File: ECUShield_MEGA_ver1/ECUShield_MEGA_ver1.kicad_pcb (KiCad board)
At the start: 2 copper layers, 101.6 x 53.3 mm, 53 parts, among them J1 Conn_02x03_Odd_Even, J10 PWM, J11 PWM, J12 Communication, J13 Conn_01x02_Pin, J14 Conn_01x02_Pin, J15 Conn_01x02_Pin, J16 Conn_01x02_Pin, J17 Conn_01x02_Pin, J18 Conn_01x02_Pin, J19 Conn_01x02_Pin, J2 Conn_01x02_Pin, J20 Conn_01x02_Pin, J3 Conn_01x02_Pin, J4 Conn_01x03_Pin, J5 Conn_01x03_Pin, J6 Conn_01x02_Pin, J7 Power, J8 Analog, J9 Analog, K1 G5Q-1, K2 G5Q-1, Q1 MTN2306AN3, Q2 MTN2306AN3, Q3 MTN2306AN3, Q4 MTN2306AN3, U1 MCP2515-xST, U2 MCP2551-I-SN, Y1 CSTCE16M0V53-R0

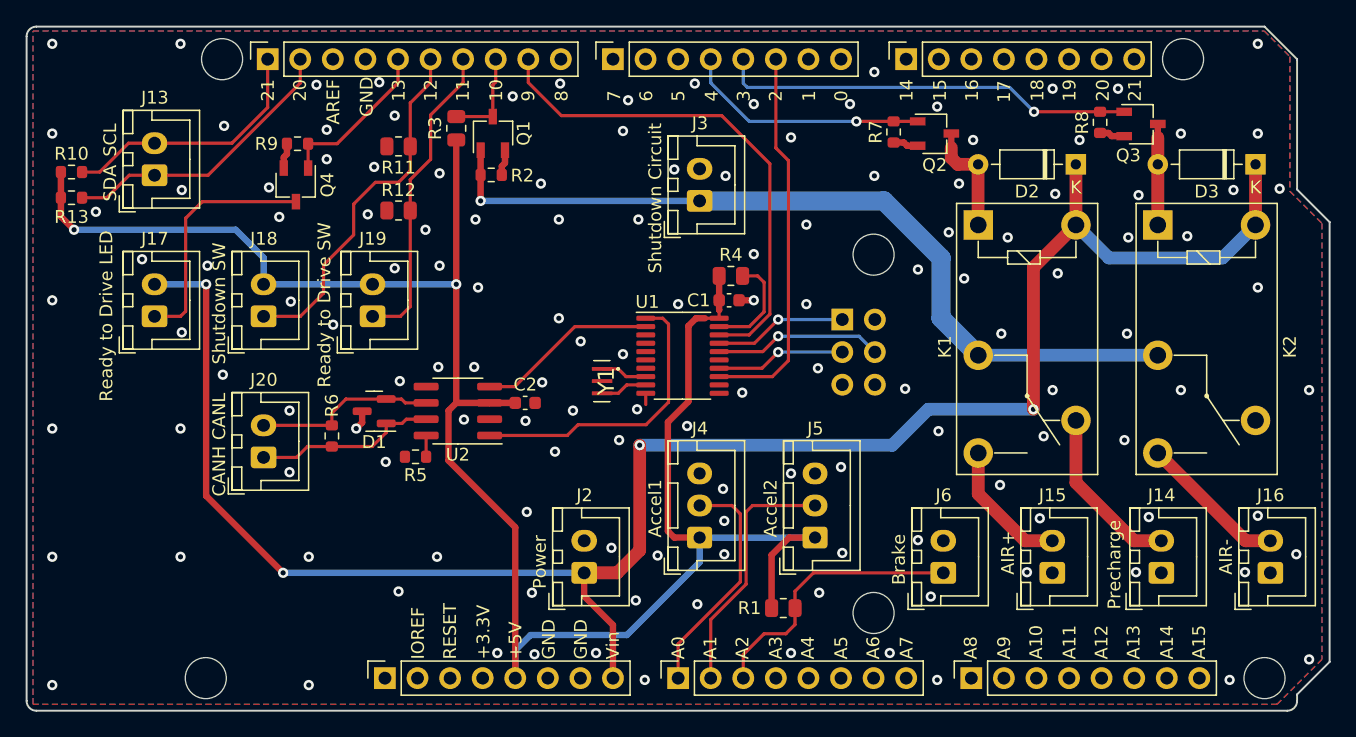
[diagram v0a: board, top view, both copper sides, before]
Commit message: 回路図修正, パターン再設計
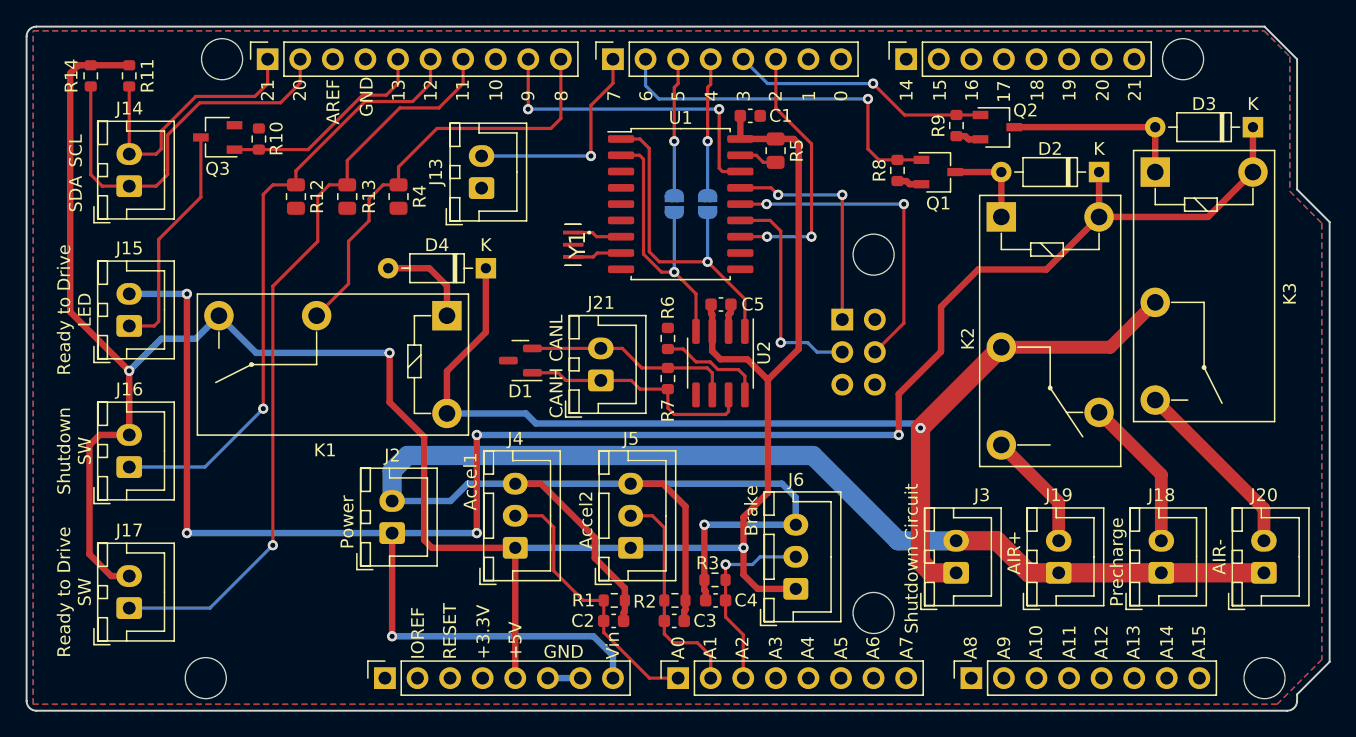
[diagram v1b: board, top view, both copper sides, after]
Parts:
- removed the K2 at (188.2, 62.1)
- removed the Q1 at (136.3, 55.0)
- added C2: 0.1u, Capacitor_SMD:C_0603_1608Metric, F.Cu at (145.8, 93.0)
- added C3: 0.1u, Capacitor_SMD:C_0603_1608Metric, F.Cu at (150.5, 93.0)
- added C4: 0.1u, Capacitor_SMD:C_0603_1608Metric, F.Cu at (153.7, 91.4)
- added D4: 1S953, Diode_THT:D_DO-35_SOD27_P7.62mm_Horizontal, F.Cu at (135.8, 65.5)
- added J13: Conn_01x02_Pin, Connector_JST:JST_XH_B2B-XH-A_1x02_P2.50mm_Vertical, F.Cu at (135.5, 59.2)
- added JP1: SolderJumper_2_Open, Jumper:SolderJumper-2_P1.3mm_Open_RoundedPad1.0x1.5mm, B.Cu at (150.5, 60.5)
- added JP2: SolderJumper_2_Open, Jumper:SolderJumper-2_P1.3mm_Open_RoundedPad1.0x1.5mm, B.Cu at (153.1, 60.5)
- added K1: G5Q-1A, Relay_THT:Relay_SPST_Omron-G5Q-1A, F.Cu at (132.8, 69.2)
- added K3: G5Q-1A, Relay_THT:Relay_SPST_Omron-G5Q-1A, F.Cu at (188.0, 58.0)
- added R4: 10k, Resistor_SMD:R_0805_2012Metric, F.Cu at (129.0, 59.9)
- J6: value Conn_01x02_Pin -> Conn_01x03_Pin; footprint Connector_JST:JST_XH_B2B-XH-A_1x02_P2.50mm_Vertical -> Connector_JST:JST_XH_B3B-XH-A_1x03_P2.50mm_Vertical
- R1, R3: value 10k -> 100k; footprint Resistor_SMD:R_0805_2012Metric -> Resistor_SMD:R_0603_1608Metric
- R2: value 1M -> 100k
- U1: value MCP2515-xST -> MCP2515-xSO; footprint Package_SO:TSSOP-20_4.4x6.5mm_P0.65mm -> Package_SO:SOIC-18W_7.5x11.6mm_P1.27mm
- moved R3 40.6 mm to (153.7, 89.8), turned to 180 degrees
- moved R2 36.1 mm to (150.6, 91.4)
- moved J3 35.2 mm to (172.5, 89.2)
- moved J17 29.6 mm to (108.0, 92.0)
- moved J21 27.0 mm to (144.8, 74.2)
- moved R7 26.6 mm to (150.0, 74.1)
- moved R6 21.7 mm to (150.0, 71.0), turned to 90 degrees
- moved U2 20.8 mm to (154.1, 72.9), turned to -90 degrees
- moved C5 17.1 mm to (154.1, 68.3)
- moved J16 15.7 mm to (108.0, 81.0)
- moved J2 15.3 mm to (128.5, 86.2)
- moved C1 14.5 mm to (156.4, 53.6)
- moved J4 14.4 mm to (138.1, 87.3)
- moved J5 14.4 mm to (147.1, 87.3)
- moved R1 13.2 mm to (145.8, 91.4)
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- renumbered C2 to C5, J13 to J14, J17 to J15, J18 to J16, J19 to J17, J14 to J18, J15 to J19, J16 to J20, J20 to J21, K1 to K2, Q2 to Q1, Q3 to Q2, Q4 to Q3, R9 to R10, R10 to R11, R11 to R12, R12 to R13, R13 to R14, R4 to R5, R5 to R6, R6 to R7, R7 to R8, R8 to R9
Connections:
- J6 pad 1: /A2 -> +5V
- J6 pad 2: GND -> /A2
- Q1 pad 1: /*4 -> /*6
- R1 pad 1: +5V -> /A0
- R1 pad 2: /A2 -> GND
- R2 pad 1: SHUTDOWN_CIRCUIT -> /A1
- R3 pad 1: +5V -> /A2
- R3 pad 2: /*10 -> GND
- R8 pad 1: /*4 -> /*6
- U1 pad 10: GND -> unconnected-(U1-~{RX1BF}-Pad10)
- U1 pad 12: unconnected-(U1-~{RX0BF}-Pad12) -> /*2/INT_A
- U1 pad 13: /*2/INT_A -> /SCK_A
- U1 pad 14: /SCK_A -> /MOSI_A
- U1 pad 15: unconnected-(U1-NC-Pad15) -> /MISO_A
- U1 pad 16: /MOSI_A -> /*9/CS_A
- U1 pad 17: /MISO_A -> Net-(U1-~{RESET})
- U1 pad 18: /*9/CS_A -> +5V
- U1 pad 7: unconnected-(U1-~{TX2RTS}-Pad7) -> /OSC2
- U1 pad 8: /OSC2 -> /OSC1
- U1 pad 9: /OSC1 -> GND
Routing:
- net GND: track 11.6 -> 167.9 mm, vias 139 -> 1
- net /*11: track 24.2 -> 59.9 mm, vias 0 -> 1
- net /*8: track 0.00 -> 33.8 mm
- net +5V: track 150.4 -> 180.4 mm, vias 2 -> 3
- net /*6: track 0.00 -> 28.3 mm, vias 0 -> 1
- net SHUTDOWN_CIRCUIT: track 64.5 -> 85.9 mm
- net /*12: track 28.2 -> 48.2 mm, vias 0 -> 1
- net /*7: track 0.00 -> 16.8 mm, vias 0 -> 1
- net /*9/CS_A: track 39.6 -> 25.2 mm, vias 0 -> 2
- net +12V: track 148.1 -> 161.0 mm, vias 4 -> 6
- net /*3: track 32.5 -> 20.3 mm
- net /MOSI_A: track 13.2 -> 25.2 mm, vias 1 -> 2
- net /*5: track 0.00 -> 10.8 mm, vias 0 -> 1
- net /*2/INT_A: track 29.8 -> 20.5 mm, vias 0 -> 2
- net /*4: track 19.2 -> 10.7 mm
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
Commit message: パターン再設計完了, 寝かせ
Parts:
- moved J2 22.7 mm to (151.0, 89.2)
- moved C2 15.5 mm to (130.9, 88.5)
- moved R1 15.5 mm to (131.0, 86.9)
- moved J4 13.0 mm to (125.5, 90.5)
- moved R3 11.5 mm to (165.1, 88.0), turned to 0 degrees
- moved C4 11.4 mm to (165.0, 89.6), turned to 0 degrees
- moved J5 8.27 mm to (139.5, 90.5)
- moved C3 6.51 mm to (144.9, 89.6)
- moved R2 6.51 mm to (145.0, 88.0)
- moved J6 0.50 mm to (159.5, 90.5)
- moved R14 0.50 mm to (105.5, 50.5)
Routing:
- net GND: track 167.9 -> 135.4 mm, vias 1 -> 116
- net +12V: track 161.0 -> 147.7 mm, vias 6 -> 5
- net /A0: track 21.4 -> 33.9 mm, vias 0 -> 2
- net +5V: track 180.4 -> 190.8 mm
- net /A1: track 17.4 -> 21.5 mm, vias 0 -> 2
- net /A2: track 15.2 -> 18.6 mm, vias 1 -> 0
- net /*11: track 59.9 -> 61.3 mm
- net /*6: track 28.3 -> 26.9 mm
- net /*3: track 20.3 -> 21.4 mm
- net /MOSI_A: track 25.2 -> 24.2 mm
- net /SDA/20: track 30.6 -> 29.7 mm
- net /SCL/21: track 21.1 -> 20.3 mm
- net /MISO_A: track 17.9 -> 17.2 mm
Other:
- board text added: "5V"
- board text removed: "+5V"

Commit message: 修正版寝かせ
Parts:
- added J22: Conn_01x02_Pin, Connector_JST:JST_XH_B2B-XH-A_1x02_P2.50mm_Vertical, F.Cu at (129.5, 59.2)
- moved R12 7.50 mm to (115.0, 64.4)
- moved R13 6.73 mm to (120.0, 64.4)
- moved R4 6.02 mm to (125.0, 64.4)
- moved J13 1.30 mm to (136.8, 59.2)
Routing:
- net /*10: track 0.00 -> 12.7 mm
- net /*12: track 48.2 -> 56.3 mm
- net /*8: track 33.6 -> 37.4 mm, vias 0 -> 2
- net /MOSI_A: track 24.2 -> 20.8 mm
- net /*11: track 61.3 -> 64.0 mm
- net GND: track 135.4 -> 133.1 mm, vias 116 -> 117
- net /*7: track 16.8 -> 15.5 mm
- net /*2/INT_A: track 20.5 -> 19.3 mm
- net /*13: track 16.8 -> 17.9 mm
- net /SCL/21: track 20.3 -> 21.0 mm
- net /SDA/20: track 29.7 -> 29.0 mm
- net /MISO_A: track 17.2 -> 17.9 mm
- net /RtD_LED: track 18.2 -> 18.8 mm

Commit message: 10k抵抗フットプリント修正2012
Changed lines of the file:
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@@
     (fp_line (start 4.95 3.4) (end 4.95 -2.35)
       (stroke (width 0.1) (type solid)) (layer "F.Fab"))
-    (pad "1" thru_hole roundrect (at 0 0 90) (size 1.7 2) (drill 1) (layers "*.Cu" "*.Mask") (roundrect_rratio 0.147059)
+    (pad "1" thru_hole roundrect (at 0 0 90) (size 1.7 2) (drill 1) (layers "*.Cu" "*.Mask") (roundrect_rratio 0.1470588235)
       (net 1 "GND") (pinfunction "Pin_1") (pintype "passive"))
     (pad "2" thru_hole oval (at 2.5 0 90) (size 1.7 2) (drill 1) (layers "*.Cu" "*.Mask")
@@
     (fp_line (start 1 0.625) (end -1 0.625)
       (stroke (width 0.1) (type solid)) (layer "F.Fab"))
-    (pad "1" smd roundrect (at -0.9125 0 270) (size 1.025 1.4) (layers "F.Cu" "F.Paste" "F.Mask") (roundrect_rratio 0.243902)
+    (pad "1" smd roundrect (at -0.9125 0 270) (size 1.025 1.4) (layers "F.Cu" "F.Paste" "F.Mask") (roundrect_rratio 0.243902439)
       (net 27 "/*8") (pintype "passive"))
-    (pad "2" smd roundrect (at 0.9125 0 270) (size 1.025 1.4) (layers "F.Cu" "F.Paste" "F.Mask") (roundrect_rratio 0.243902)
+    (pad "2" smd roundrect (at 0.9125 0 270) (size 1.025 1.4) (layers "F.Cu" "F.Paste" "F.Mask") (roundrect_rratio 0.243902439)
       (net 1 "GND") (pintype "passive"))
     (model "${KICAD6_3DMODEL_DIR}/Resistor_SMD.3dshapes/R_0805_2012Metric.wrl"
@@
     (fp_line (start 7.45 3.4) (end 7.45 -2.35)
       (stroke (width 0.1) (type solid)) (layer "F.Fab"))
-    (pad "1" thru_hole roundrect (at 0 0 90) (size 1.7 1.95) (drill 0.95) (layers "*.Cu" "*.Mask") (roundrect_rratio 0.147059)
+    (pad "1" thru_hole roundrect (at 0 0 90) (size 1.7 1.95) (drill 0.95) (layers "*.Cu" "*.Mask") (roundrect_rratio 0.1470588235)
       (net 4 "+5V") (pinfunction "Pin_1") (pintype "passive"))
     (pad "2" thru_hole oval (at 2.5 0 90) (size 1.7 1.95) (drill 0.95) (layers "*.Cu" "*.Mask")
@@
     (fp_line (start 4.95 3.4) (end 4.95 -2.35)
       (stroke (width 0.1) (type solid)) (layer "F.Fab"))
-    (pad "1" thru_hole roundrect (at 0 0 90) (size 1.7 2) (drill 1) (layers "*.Cu" "*.Mask") (roundrect_rratio 0.147059)
+    (pad "1" thru_hole roundrect (at 0 0 90) (size 1.7 2) (drill 1) (layers "*.Cu" "*.Mask") (roundrect_rratio 0.1470588235)
       (net 1 "GND") (pinfunction "Pin_1") (pintype "passive"))
     (pad "2" thru_hole oval (at 2.5 0 90) (size 1.7 2) (drill 1) (layers "*.Cu" "*.Mask")
